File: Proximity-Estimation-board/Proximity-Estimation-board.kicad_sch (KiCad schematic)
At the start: 19 parts, among them Q1 TEPT4400, Q2 TEPT4400, U1 ArduinoNano33BLE, U2 OPA340P, U3 HC-SR04, U4 OPA340P

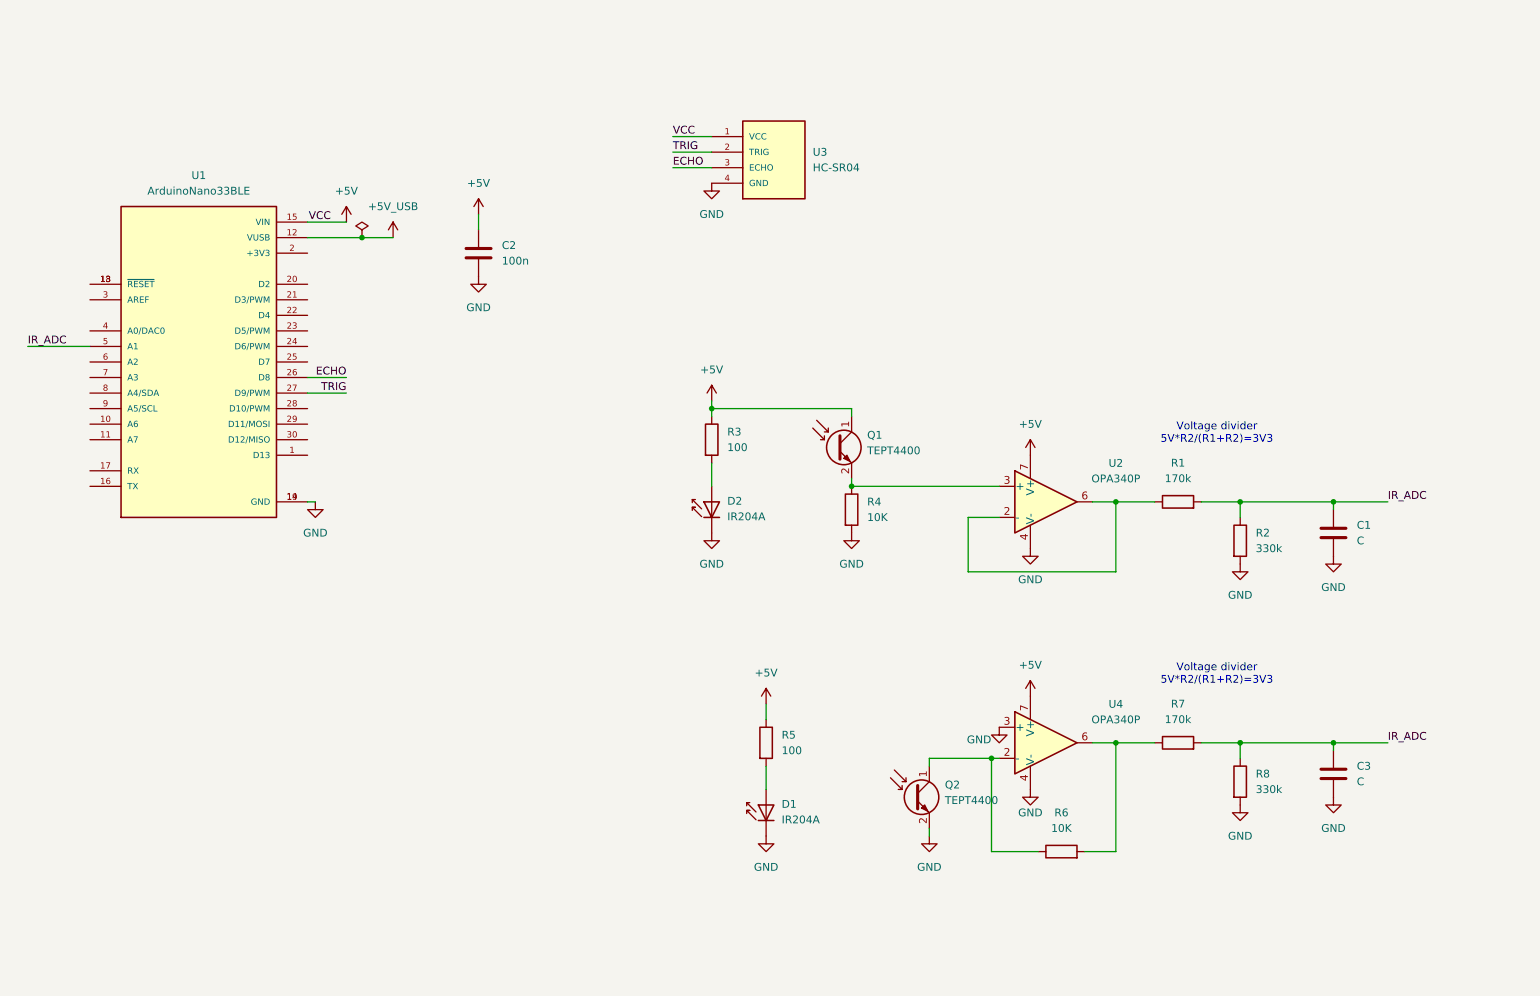
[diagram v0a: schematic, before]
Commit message: update schematic
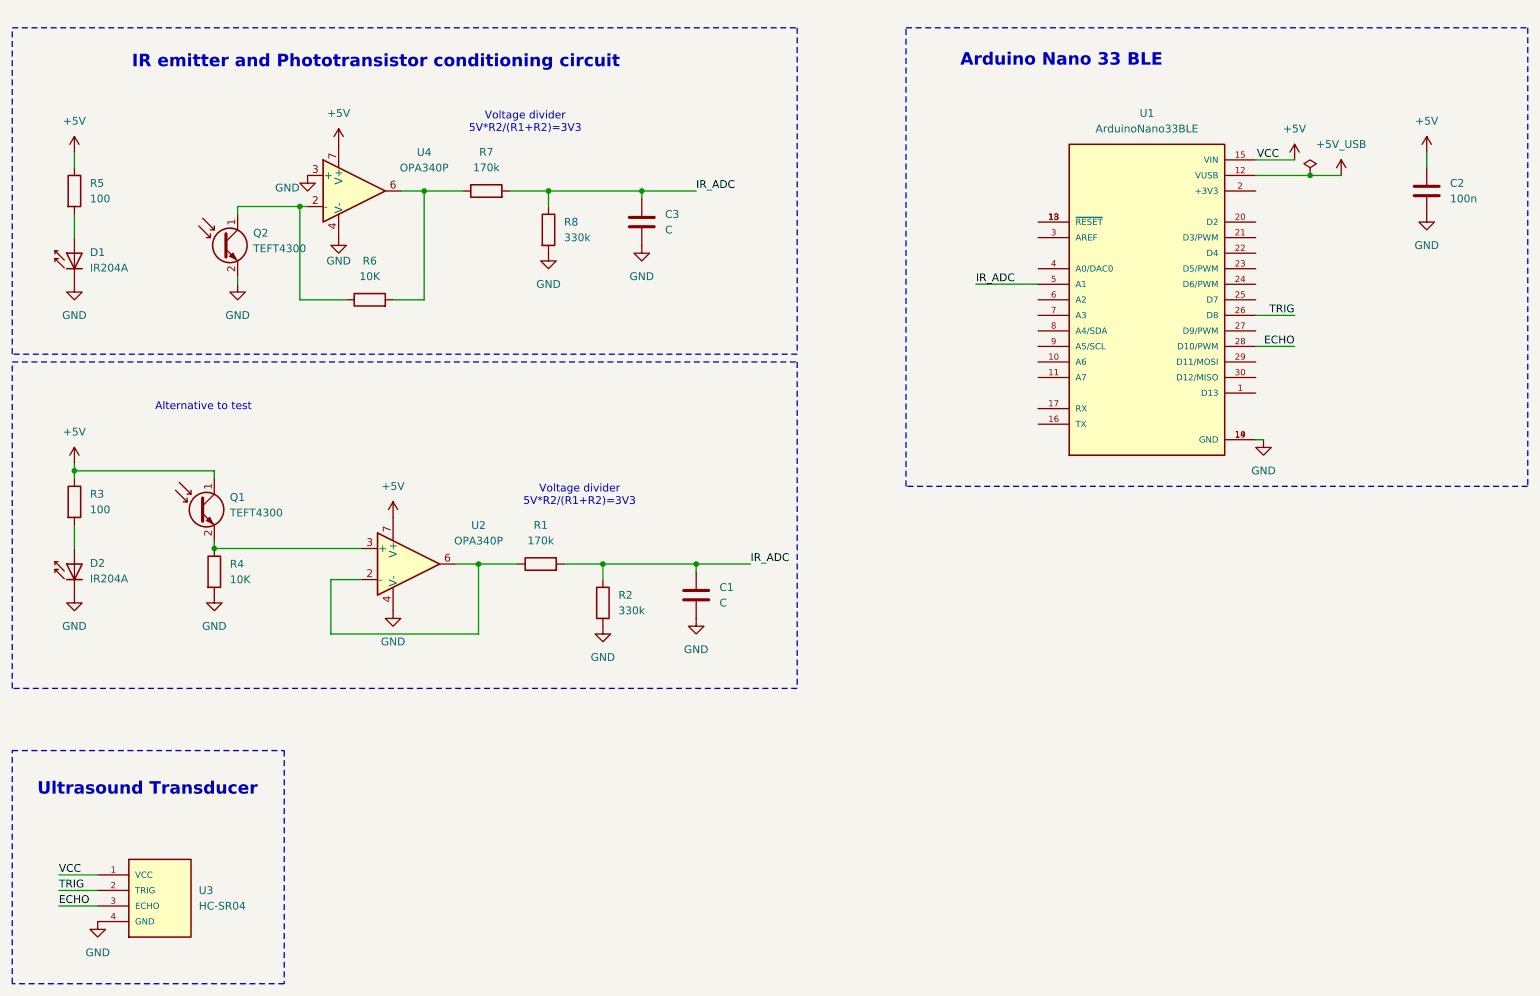
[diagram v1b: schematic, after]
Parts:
- Q1, Q2: value TEPT4400 -> TEFT4300
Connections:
- net ECHO: now also U1.28 (D10/PWM); no longer U1.26 (D8)
- net TRIG: now also U1.26 (D8); no longer U1.27 (D9/PWM)
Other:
- note added: "Alternative to test"
- note added: "Arduino Nano 33 BLE"
- note added: "IR emitter and Phototransistor conditioning circuit"
- note added: "Ultrasound Transducer"
- moved on the sheet: C1, C2, C3, D1, D2, Q1, Q2, R1, R2, R3, R4, R5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

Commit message: final schematic
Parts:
- removed C3: C, symbol Device:C
- removed D2: IR204A, LED_THT:LED_D3.0mm_IRBlack, symbol LED:IR204A
- removed Q1: TEFT4300, LED_THT:LED_D3.0mm_Clear, symbol Sensor_Optical:TEPT4400
- removed R2, R8: 330k, symbol Device:R
- removed R3: 100, symbol Device:R
- removed R4, R6: 10K, symbol Device:R
- removed R7: 170k, symbol Device:R
- removed U2: OPA340P, Package_DIP:DIP-8_W7.62mm, symbol Amplifier_Operational:OPA340P
- C1: value C -> 10nF
- R1: value 170k -> 1M
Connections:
- net +5V: no longer U4.7 (V+)
- net GND: no longer C1.2
- net IR_ADC: now also C1.2, U4.6; no longer C1.1
- net at R1.1: now also C1.1, Q2.1 (C), U4.2 (-)
- net +3V3: now reaches U1.2 (+3V3)
- net +3V3: now also U4.7 (V+)
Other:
- note removed: "Alternative to test"
- note removed: "Voltage divider 5V*R2/(R1+R2)=3V3"
- moved on the sheet: C2, D1, Q2, R5, U1, U3, U4

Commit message: add kicad schematic pdf
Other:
- company: (none) -> Lisa Santarossa
- title: (none) -> Proximity-Estimation-board
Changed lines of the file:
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@@
 	(generator_version "8.0")
 	(paper "A4")
+	(title_block
+		(title "Proximity-Estimation-board")
+		(date "2024-11-20")
+		(rev "1.0")
+		(company "Lisa Santarossa")
+	)
 	(junction
 		(at 95.25 44.45)
@@
 	(rectangle
 		(start 157.48 21.59)
-		(end 264.16 74.93)
+		(end 247.65 74.93)
 		(stroke
 			(width 0)
@@
 	(text "IR emitter and Phototransistor conditioning circuit\n"
 		(exclude_from_sim no)
-		(at 215.646 25.908 0)
+		(at 202.184 25.908 0)
 		(effects
 			(font
@@
 		(on_board yes)
 		(dnp no)
-		(fields_autoplaced yes)
 		(property "Reference" "Q2"
-			(at 195.58 53.8606 0)
+			(at 195.58 57.15 0)
 			(effects
 				(font
@@
 		)
 		(property "Value" "TEFT4300"
-			(at 195.58 56.4006 0)
-			(effects
-				(font
+			(at 193.802 59.944 0)
+			(effects
+				(font
